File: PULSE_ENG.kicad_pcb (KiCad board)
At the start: 4 copper layers, 146.7 x 93.9 mm, 145 parts, among them IC1 TPS7B8733QDDARQ1, IC2 TPS7B8750QDDARQ1, IC28 INA226AIDGSR, IC29 TPS25940ARVCR, IC30 TPS25940ARVCR, IC31 INA226AIDGSR, J10 Screw_Terminal_01x01, J11 Screw_Terminal_01x04, J12 Screw_Terminal_01x04, J13 TC2050-IDC-NL, J8 Screw_Terminal_01x04, J9 Screw_Terminal_01x06, U1 ATSAMD21J17D-M, U2 LT6108IMS8-1-TRPBF, U3 LM139ADRG4, U4 EPC2152, U5 LT6108IMS8-1-TRPBF

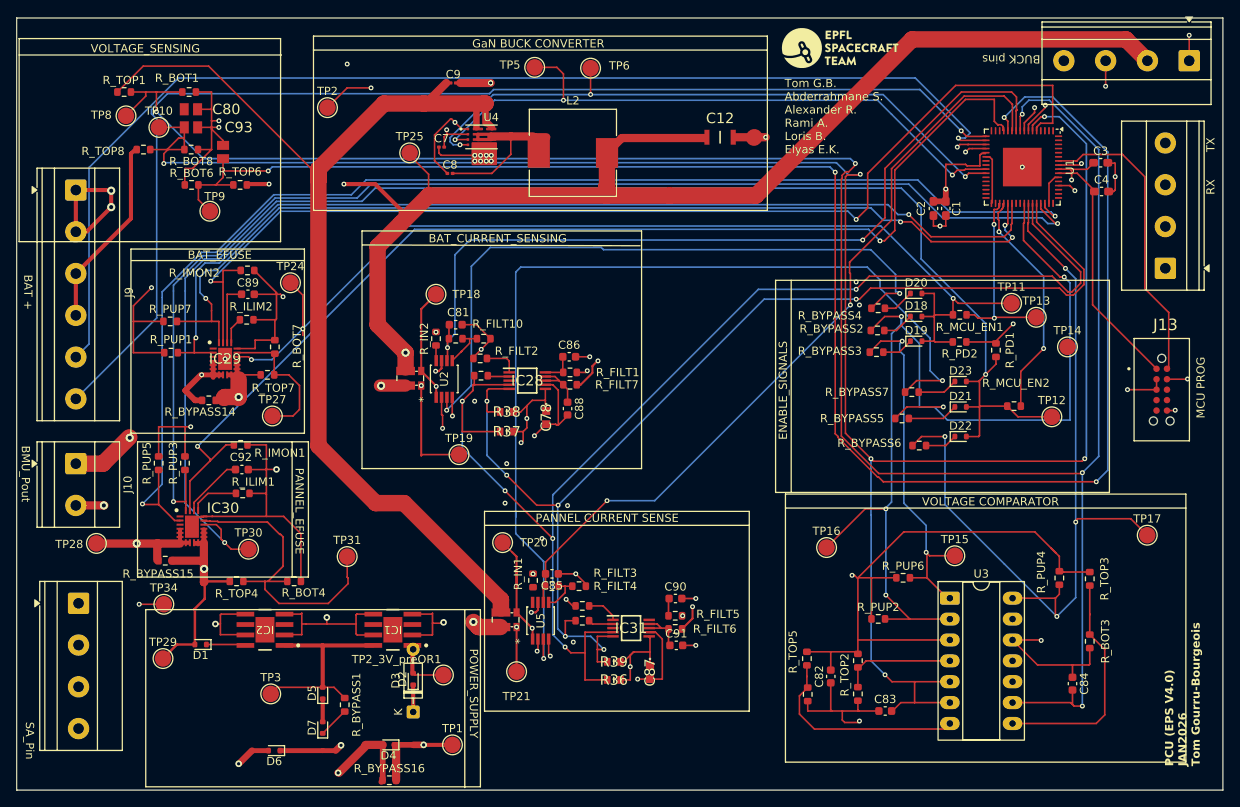
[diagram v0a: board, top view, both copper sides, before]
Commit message: fixed LDO
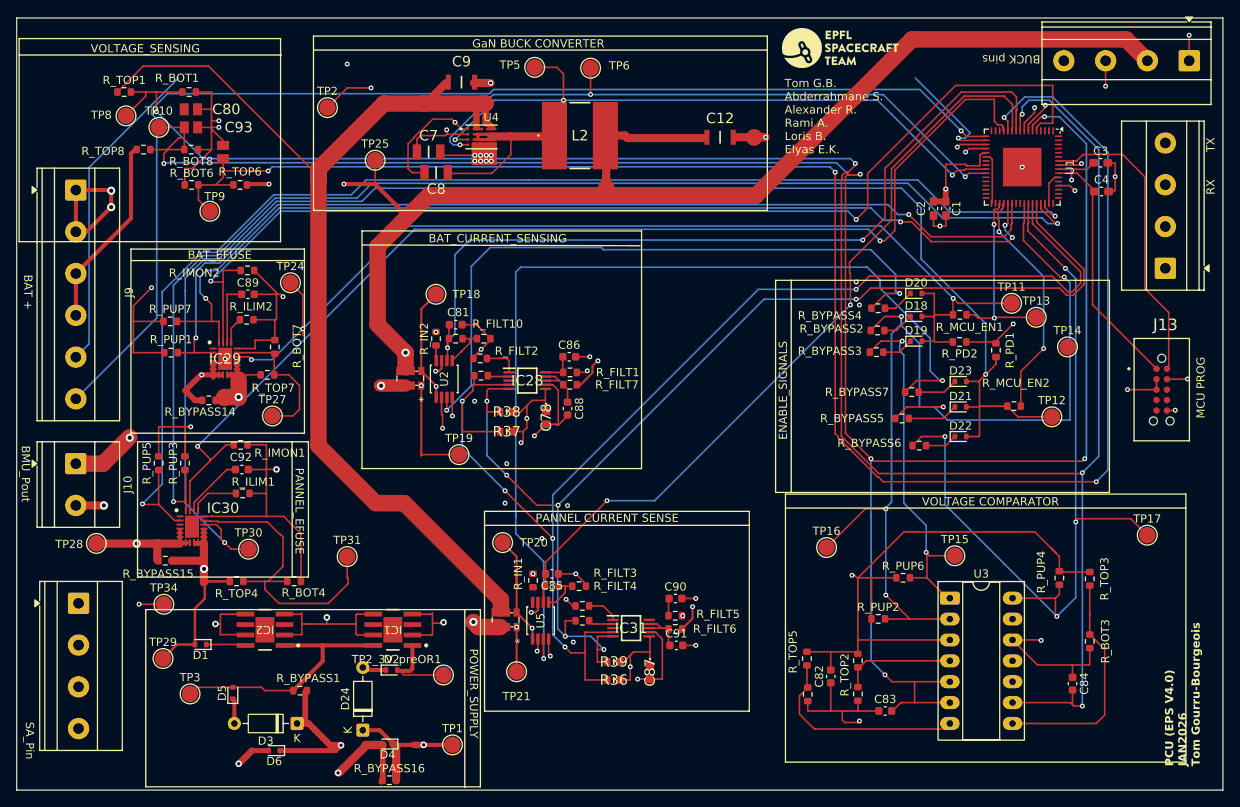
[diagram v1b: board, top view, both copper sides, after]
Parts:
- removed D7: 1N4148WT, Diode_SMD:D_SOD-523
- added D24: 1N5711, Diode_THT:D_DO-35_SOD27_P7.62mm_Horizontal, F.Cu at (71.5, 142.8)
- C7, C8: value 100nF -> CAPC3216X170N; footprint Capacitor_SMD:C_0201_0603Metric -> PULSE_Library:CAPC3216X170N
- C9: footprint Capacitor_SMD:C_0201_0603Metric -> PULSE_Library:CAPC3216X180N
- L2: value 47 -> 78404084470; footprint Inductor_SMD:L_10.4x10.4_H4.8 -> PULSE_Library:78404084470
- moved D3 14.2 mm to (63.5, 142.0), turned to 180 degrees
- moved D5 10.9 mm to (55.7, 138.3)
- moved TP3 9.81 mm to (50.5, 138.4)
- moved R_BYPASS1 5.70 mm to (63.9, 138.0), turned to 0 degrees
- moved TP25 4.30 mm to (73.0, 73.5)
- moved D2 2.84 mm to (75.0, 135.5), turned to 0 degrees
- moved L2 2.27 mm to (97.9, 70.5)
- moved C7 1.69 mm to (79.5, 72.5)
- moved C8 1.68 mm to (80.4, 75.0), turned to 180 degrees
- moved C9 1.01 mm to (83.5, 64.0)
- moved D4 0.16 mm to (74.5, 144.5)
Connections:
- C1 pad 1: VDDIN -> VDDANA
- C2 pad 1: VDDIN -> VDDANA
- C3 pad 1: VDDIN -> VDDANA
- C4 pad 1: VDDIN -> VDDANA
- C7 pad 1: GND -> 12V_1
- C7 pad 2: 12V_1 -> GND
- C8 pad 1: Net-(J11-Pin_3) -> Net-(C8-Pad2)
- C8 pad 2: Net-(C8-Pad2) -> Net-(J11-Pin_3)
- C82 pad 1: VDDIN -> VDDANA
- C87 pad 1: VDDIN -> VDDANA
- C9 pad 1: /V_pannel_protected -> Net-(C12-Pad1)
- C9 pad 2: Net-(C12-Pad1) -> /V_pannel_protected
- D4 pad 1: VDDIN -> VDDANA
- IC31 pad 6: VDDIN -> VDDANA
- J10 pad 2: GND -> (no net)
- J13 pad 1: VDDIN -> VDDANA
- R36 pad 2: VDDIN -> VDDANA
- R39 pad 2: VDDIN -> VDDANA
- R_BYPASS16 pad 2: VDDIN -> VDDANA
- R_PUP2 pad 1: VDDIN -> VDDANA
- R_PUP3 pad 2: VDDIN -> VDDANA
- R_PUP4 pad 2: VDDIN -> VDDANA
- R_PUP5 pad 2: VDDIN -> VDDANA
- R_PUP6 pad 1: VDDIN -> VDDANA
- R_TOP2 pad 2: VDDIN -> VDDANA
- R_TOP3 pad 2: VDDIN -> VDDANA
- R_TOP5 pad 2: VDDIN -> VDDANA
- TP1 pad 1: VDDIN -> VDDANA
- U1 pad 21: VDDIN -> VDDANA
- U1 pad 56: VDDIN -> VDDANA
- U1 pad 8: VDDIN -> VDDANA
- U2 pad 2: /3.3V -> VDDANA
- U3 pad 3: VDDIN -> VDDANA
- U5 pad 2: VDDIN -> VDDANA
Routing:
- net /POWER_SWITCH: track 143.3 -> 53.7 mm
- net VDDIN: track 24.6 -> 0.00 mm
- net (no net): track 3.34 -> 27.9 mm
- net VDDANA: track 0.00 -> 9.12 mm
- net /5V: track 25.3 -> 32.9 mm
- net /EPS_Power_Supply/5V_LDO: track 25.7 -> 30.8 mm
- net Net-(C8-Pad2): track 21.5 -> 25.7 mm
- net Net-(C12-Pad1): track 7.97 -> 4.02 mm, vias 3 -> 1
- net 12V_1: track 131.8 -> 135.5 mm
- net Net-(J11-Pin_3): track 94.6 -> 98.2 mm
- net Net-(D3-A): track 0.00 -> 3.08 mm
- net Net-(D5-K): track 2.80 -> 0.00 mm
- net /EPS_Power_Supply/3V3_LDO: track 7.19 -> 9.97 mm
- net /V_pannel_protected: track 132.0 -> 134.3 mm, vias 0 -> 2
- net /3.3V: track 555.0 -> 552.9 mm
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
